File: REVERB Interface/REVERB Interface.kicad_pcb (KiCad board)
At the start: 2 copper layers, 23 parts, among them J1 RPiZeroW, J10 USB, J2 Iridium, J3 APRS, J4 Antenna, J5 MAX3232BOB, J6 USBSER2, J7 USBSER3, J8 USBSER1, J9 USB, M1 MountingHole_Pad, M2 MountingHole_Pad, M3 MountingHole_Pad, M4 MountingHole_Pad, U2 MAX3232, U3 SC16IS752IPW

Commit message: copy old board layout positions
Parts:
- H1, H2, J1, J2, J3: moved to B.Cu
- moved J9 94.0 mm to (164.7, 177.2)
- moved J10 94.0 mm to (160.1, 182.7)
- moved U3 94.0 mm to (177.6, 168.7)
- moved J5 94.0 mm to (141.2, 165.4)
- moved J6 94.0 mm to (136.6, 165.4)
- moved J7 94.0 mm to (160.1, 165.4)
- moved J8 94.0 mm to (132.0, 165.4)
- moved J1 73.6 mm to (168.8, 132.3)
- moved J2 70.9 mm to (123.2, 134.6)
- moved M2 63.1 mm to (189.4, 57.9)
- moved M4 63.1 mm to (191.9, 143.7)
- moved J4 58.1 mm to (114.0, 65.6)
- moved U2 58.1 mm to (141.6, 127.6)
- moved M1 53.5 mm to (115.7, 57.9)
- moved M3 42.1 mm to (111.9, 143.7)
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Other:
- board outline added: 90.2 x 95.9 mm

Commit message: silkscreen labels
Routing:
- added copper zone on B.Cu, net GND
- added copper zone on F.Cu, net GND
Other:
- board text added: ". ."
- board text added: "1 ."
- board text added: "10 9"
- board text added: "12V 12V"
- board text added: "2 G"
- board text added: "3V3 3V3"
- board text added: "4 3"
- board text added: "5V 5V"
- board text added: "7 6"
- board text added: "8 G"
- board text added: "BATV"
- board text added: "BATV BATV"
- board text added: "BCR BCR"
- board text added: "G ."
- board text added: "G 5"
- board text added: "G G"
- board text added: "GND"
- board text added: "PCM PCM"
- board text added: "RX"
- board text added: "SCL"
- board text added: "SDA"
- board text added: "TX"

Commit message: do stuff
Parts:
- removed J5: MAX3232BOB, Connector_PinSocket_2.54mm:PinSocket_1x10_P2.54mm_Vertical
- removed U3: SC16IS752IPW, Package_SO:TSSOP-28_4.4x9.7mm_P0.65mm
- moved J6 79.4 mm to (137.9, 86.1)
- moved J7 79.4 mm to (161.4, 86.1)
- moved J8 79.4 mm to (133.3, 86.1)
- moved J10 42.0 mm to (156.2, 141.0), turned to 90 degrees
- moved J9 39.4 mm to (176.5, 139.7)
- moved C4 19.9 mm to (129.5, 130.8)
- moved C2 19.1 mm to (128.9, 126.8), turned to 270 degrees
- moved C1 17.1 mm to (128.9, 122.6), turned to 90 degrees
- moved C5 10.5 mm to (143.9, 123.2), turned to 270 degrees
- moved C3 5.63 mm to (136.5, 119.4), turned to 270 degrees
- moved U2 4.49 mm to (137.2, 127.0)

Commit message: bunch of work
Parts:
- removed the J7 at (161.4, 86.1)
- removed J8: USBSER1, Connector_PinSocket_2.54mm:PinSocket_1x12_P2.54mm_Vertical
- removed J9: USB, Connector_PinSocket_2.54mm:PinSocket_1x02_P2.54mm_Vertical
- added C6: 4.7uF, Capacitor_SMD:C_0805_2012Metric_Pad1.18x1.45mm_HandSolder, F.Cu at (160.0, 163.8)
- added C7: 0.1uF, Capacitor_SMD:C_0805_2012Metric_Pad1.18x1.45mm_HandSolder, F.Cu at (166.0, 159.1)
- added C8: 1uF, Capacitor_SMD:C_0805_2012Metric_Pad1.18x1.45mm_HandSolder, F.Cu at (160.0, 160.8)
- added D1: RED, LED_SMD:LED_0805_2012Metric_Pad1.15x1.40mm_HandSolder, F.Cu at (164.8, 162.1)
- added D2: GREEN, LED_SMD:LED_0805_2012Metric_Pad1.15x1.40mm_HandSolder, F.Cu at (160.0, 166.9)
- added D3: RED, LED_SMD:LED_0805_2012Metric_Pad1.15x1.40mm_HandSolder, F.Cu at (166.1, 167.6)
- added D4: RED, LED_SMD:LED_0805_2012Metric_Pad1.15x1.40mm_HandSolder, F.Cu at (135.9, 107.9)
- added D5: RED, LED_SMD:LED_0805_2012Metric_Pad1.15x1.40mm_HandSolder, F.Cu at (151.5, 118.7)
- added D6: GREEN, LED_SMD:LED_0805_2012Metric_Pad1.15x1.40mm_HandSolder, F.Cu at (145.4, 111.1)
- added R1: 1K, Resistor_SMD:R_1206_3216Metric_Pad1.30x1.75mm_HandSolder, F.Cu at (166.5, 155.9)
- added R2: 1K, Resistor_SMD:R_1206_3216Metric_Pad1.30x1.75mm_HandSolder, F.Cu at (160.6, 157.7)
- added R3: 1K, Resistor_SMD:R_1206_3216Metric_Pad1.30x1.75mm_HandSolder, F.Cu at (160.6, 154.4)
- added R4: 1K, Resistor_SMD:R_1206_3216Metric_Pad1.30x1.75mm_HandSolder, F.Cu at (130.5, 111.3)
- added R5: 1K, Resistor_SMD:R_1206_3216Metric_Pad1.30x1.75mm_HandSolder, F.Cu at (145.4, 118.7)
- added R6: 1K, Resistor_SMD:R_1206_3216Metric_Pad1.30x1.75mm_HandSolder, F.Cu at (145.4, 115.6)
- added U1: LSM9DS1BOB, REVERB Interface:LSM9DS1BOB, F.Cu at (145.4, 82.5)
- added U3: CY7C65213-28PVXI, Package_SO:SSOP-28_5.3x10.2mm_P0.65mm, F.Cu at (156.4, 132.5)
- J6: value USBSER2 -> USB_B_Micro; footprint Connector_PinSocket_2.54mm:PinSocket_1x12_P2.54mm_Vertical -> REVERB Interface:AdafruitMicroB
- moved J6 59.9 mm to (152.4, 144.1), turned to 180 degrees
- moved J7 27.1 mm to (182.9, 135.9)
- renumbered J10 to J7
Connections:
- H2 pad 19: (no net) -> /SW9
- J6 pad 1: (no net) -> /SW7
- J6 pad 2: (no net) -> /D-
- J6 pad 3: (no net) -> /D+
- J6 pad 5: (no net) -> GND
- J6 pad 6: (no net) -> GND

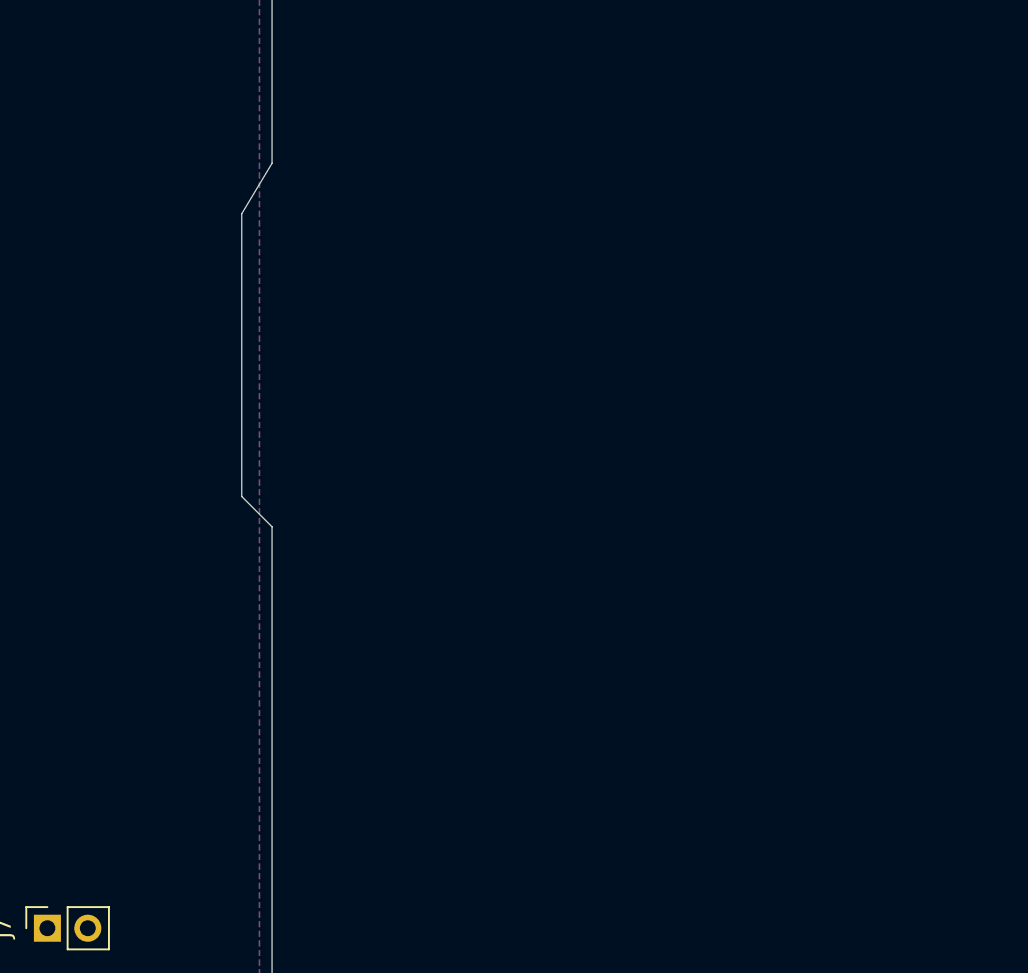
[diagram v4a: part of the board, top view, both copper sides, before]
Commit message: add solder jumpers
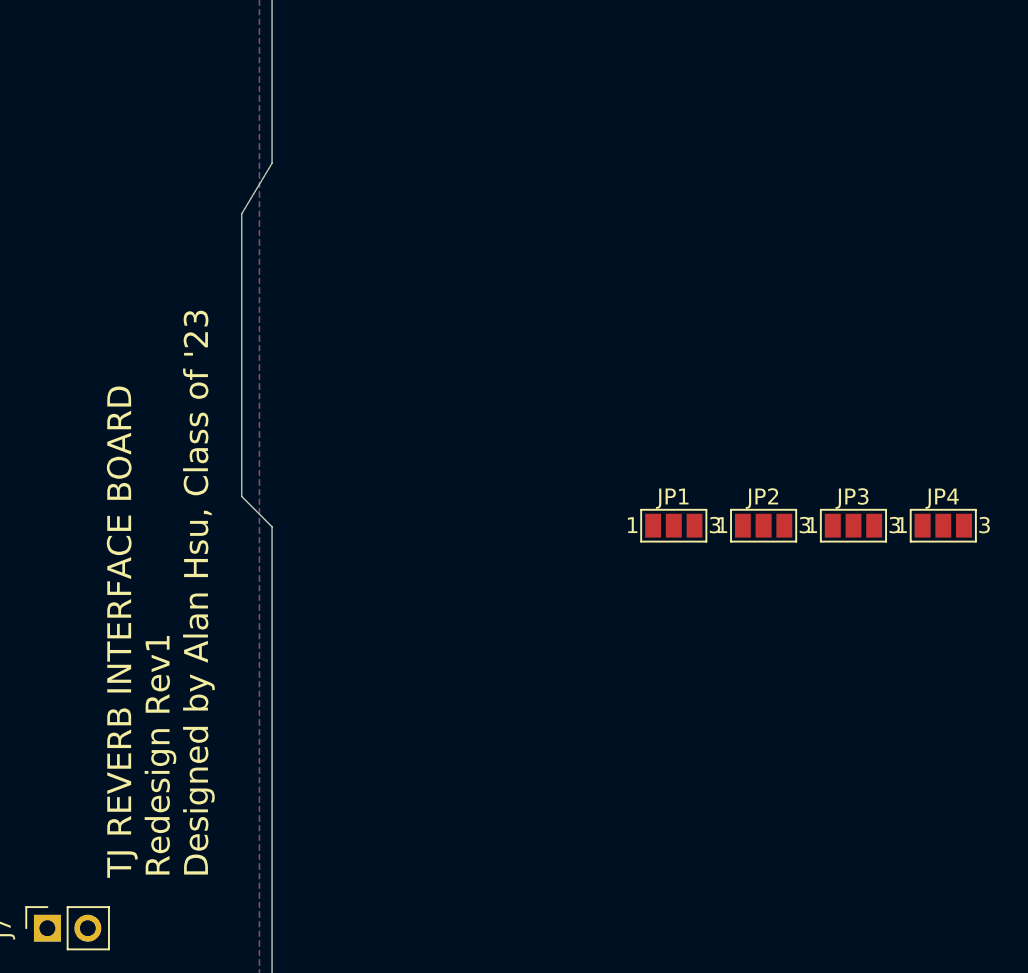
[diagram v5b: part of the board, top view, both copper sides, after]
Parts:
- added JP1: HWRX, Jumper:SolderJumper-3_P1.3mm_Open_Pad1.0x1.5mm_NumberLabels, F.Cu at (222.3, 110.6)
- added JP2: HWTX, Jumper:SolderJumper-3_P1.3mm_Open_Pad1.0x1.5mm_NumberLabels, F.Cu at (227.9, 110.6)
- added JP3: USBUARTRX, Jumper:SolderJumper-3_P1.3mm_Open_Pad1.0x1.5mm_NumberLabels, F.Cu at (233.6, 110.6)
- added JP4: USBUARTTX, Jumper:SolderJumper-3_P1.3mm_Open_Pad1.0x1.5mm_NumberLabels, F.Cu at (239.2, 110.6)
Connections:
- D1 pad 1: /APRSTX -> /USBUARTTX
- D2 pad 1: /APRSRX -> /USBUARTRX
- J1 pad 10: /R1OUT -> /HWRX
- J1 pad 8: /T1IN -> /HWTX
- U3 pad 1: /APRSTX -> /USBUARTTX
- U3 pad 5: /APRSRX -> /USBUARTRX
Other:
- board text added: "TJ REVERB INTERFACE BOARD Redesign Rev1 Designed by Alan Hsu, Class of '23"

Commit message: routing work
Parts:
- R1, R2, R3, R4, R5, R6: footprint Resistor_SMD:R_1206_3216Metric_Pad1.30x1.75mm_HandSolder -> Resistor_SMD:R_0805_2012Metric_Pad1.20x1.40mm_HandSolder
- moved D3 101.4 mm to (137.2, 70.5), turned to 180 degrees
- moved R3 88.8 mm to (131.4, 70.6)
- moved JP1 82.3 mm to (140.4, 102.3)
- moved JP2 82.3 mm to (146.0, 102.3)
- moved JP3 82.3 mm to (151.7, 102.3)
- moved JP4 82.3 mm to (157.3, 102.3)
- moved R4 40.1 mm to (142.9, 73.2)
- moved D4 38.7 mm to (142.9, 69.8)
- moved D2 37.4 mm to (136.5, 137.8), turned to 270 degrees
- moved C6 35.9 mm to (149.2, 129.5), turned to 270 degrees
- moved C7 35.6 mm to (146.1, 129.5), turned to 270 degrees
- moved D1 31.5 mm to (144.8, 137.8), turned to 270 degrees
- moved R2 28.8 mm to (139.7, 137.8), turned to 270 degrees
- moved R1 26.0 mm to (148.0, 137.8), turned to 270 degrees
- moved C8 24.0 mm to (163.8, 137.2), turned to 270 degrees
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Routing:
- net +5V: track 0.00 -> 95.2 mm
- net /SW7: track 0.00 -> 15.8 mm
- net GND: track 0.00 -> 10.4 mm
- net /D-: track 0.00 -> 9.60 mm
- net /D+: track 0.00 -> 8.49 mm
- net Net-(C3-Pad2): track 0.00 -> 6.37 mm
- net Net-(C4-Pad2): track 0.00 -> 4.77 mm
- net Net-(C8-Pad1): track 0.00 -> 4.72 mm
- net Net-(C1-Pad1): track 0.00 -> 4.25 mm
- net Net-(C2-Pad2): track 0.00 -> 4.05 mm
- net Net-(C1-Pad2): track 0.00 -> 4.05 mm
- net Net-(C2-Pad1): track 0.00 -> 3.72 mm
- net /SW8: track 0.00 -> 3.16 mm
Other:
- board text added: "Programming USB Header"
- board text added: "THIS SIDE DOWN"
- board text added: "THIS SIDE UP"

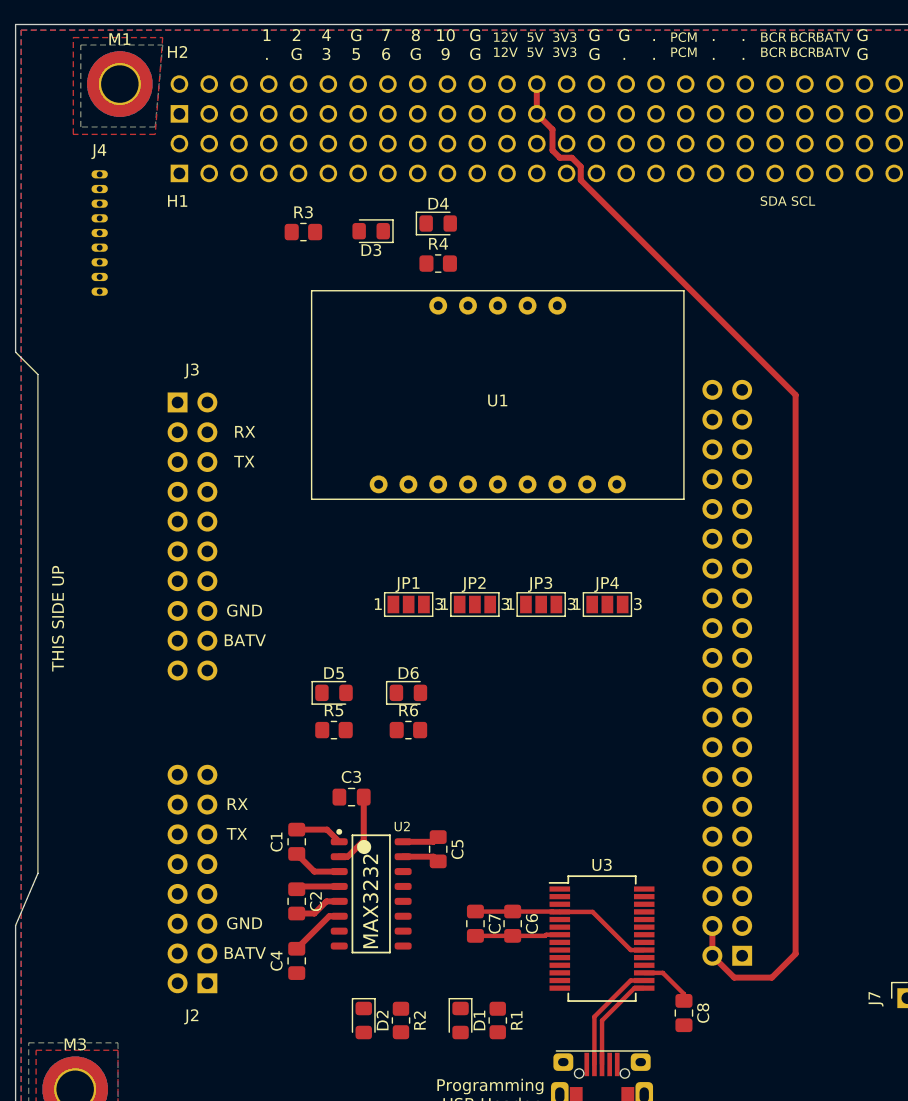
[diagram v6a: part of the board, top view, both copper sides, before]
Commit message: Update REVERB Interface.kicad_pcb
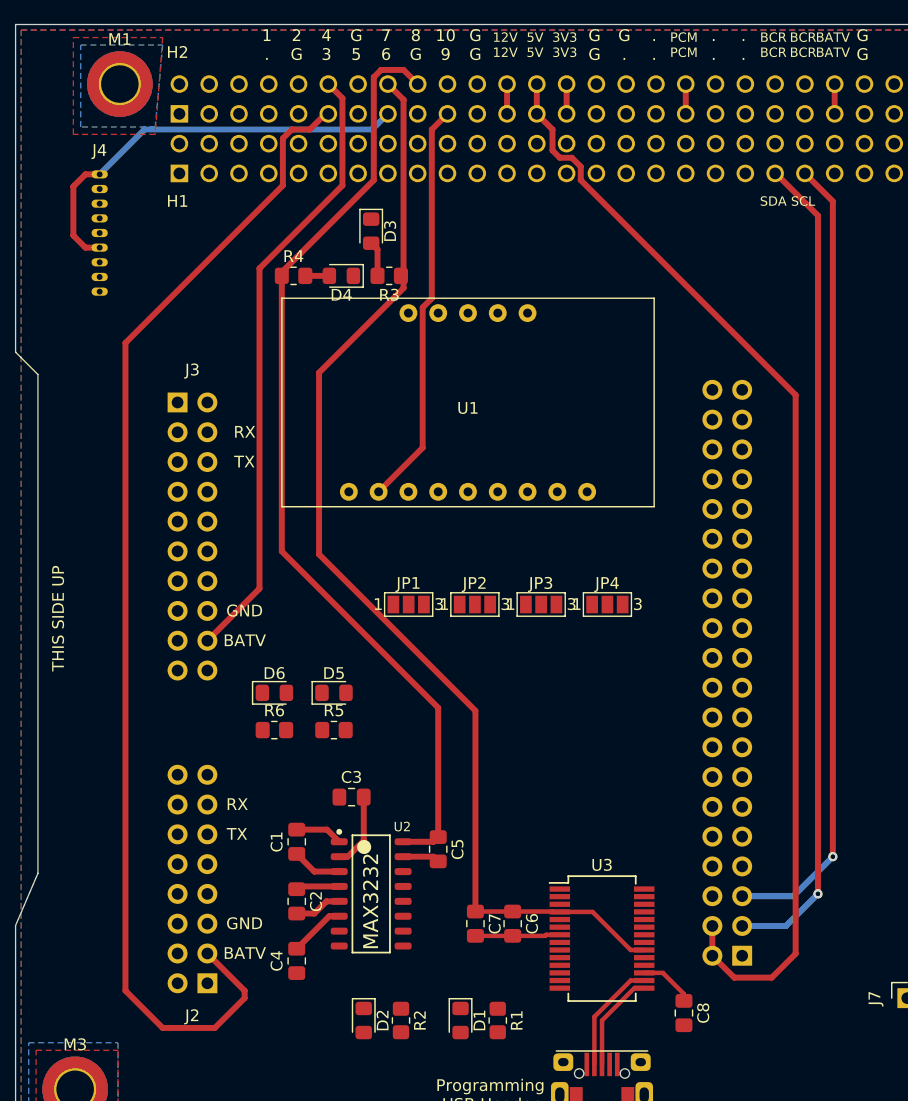
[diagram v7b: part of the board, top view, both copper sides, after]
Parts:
- moved R4 12.4 mm to (130.5, 74.3)
- moved D6 11.4 mm to (128.9, 109.9)
- moved R6 11.4 mm to (128.9, 113.0)
- moved D4 9.39 mm to (134.6, 74.3), turned to 180 degrees
- moved R3 8.22 mm to (138.7, 74.3), turned to 180 degrees
- moved U1 2.62 mm to (145.4, 85.1)
- turned D3 to 270 degrees
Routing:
- net /SW3: track 0.00 -> 100.6 mm
- net /SW7: track 15.8 -> 95.4 mm
- net /SW8: track 3.16 -> 81.2 mm
- net /EPSSDA: track 0.00 -> 70.6 mm, vias 0 -> 1
- net /EPSSCL: track 0.00 -> 68.4 mm, vias 0 -> 1
- net /SW4: track 0.00 -> 52.7 mm
- net /SW6: track 0.00 -> 36.2 mm
- net /SW9: track 0.00 -> 34.7 mm
- net Net-(D3-Pad2): track 0.00 -> 3.01 mm
- net VBUS: track 0.00 -> 2.54 mm
- net /PCM_IN: track 0.00 -> 2.54 mm
- net +3V3: track 0.00 -> 2.54 mm
- net +12V: track 0.00 -> 2.54 mm
- net Net-(D4-Pad2): track 0.00 -> 2.06 mm

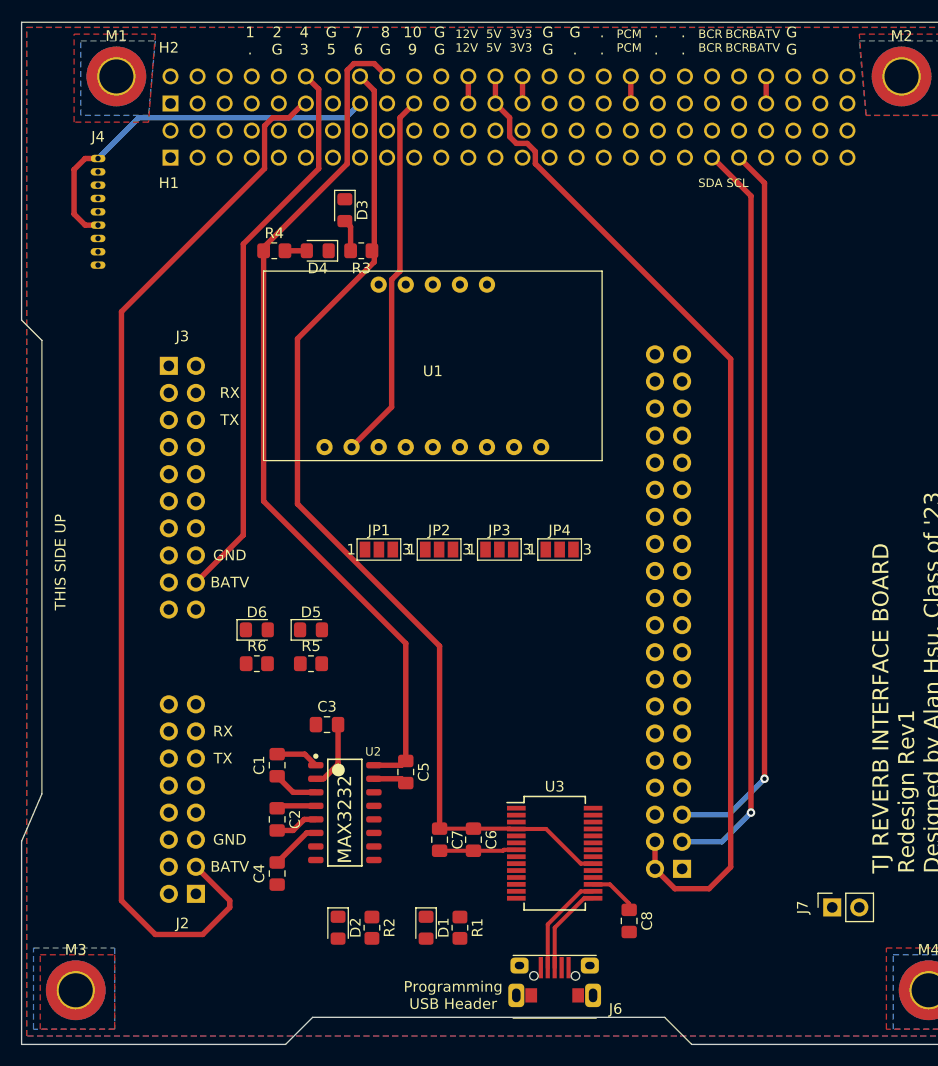
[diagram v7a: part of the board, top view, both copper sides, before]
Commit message: finsihing up routing
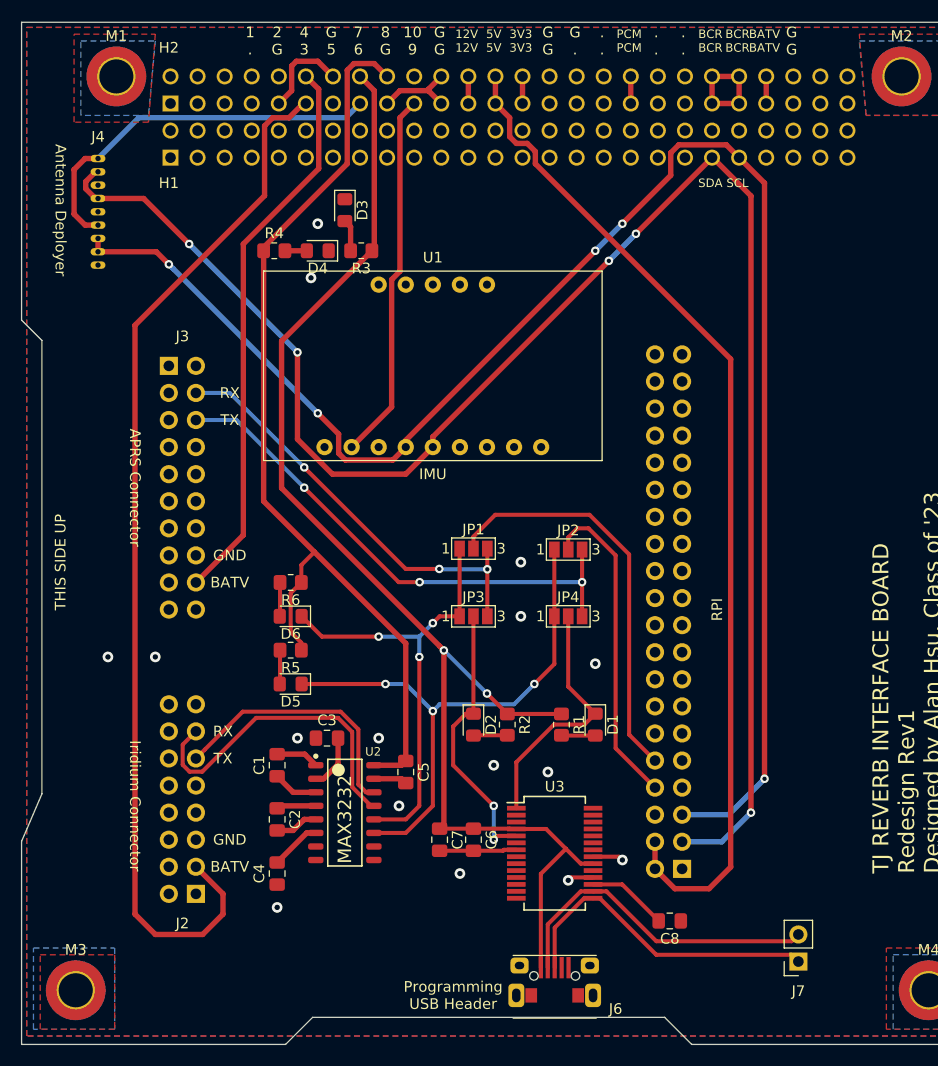
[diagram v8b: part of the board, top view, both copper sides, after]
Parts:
- moved D1 24.8 mm to (160.7, 118.7)
- moved R2 22.9 mm to (152.4, 118.7)
- moved D2 22.9 mm to (149.2, 118.7)
- moved R1 21.3 mm to (157.5, 118.7)
- moved JP2 12.1 mm to (158.1, 102.3)
- moved JP1 8.87 mm to (149.2, 102.2)
- moved R6 8.26 mm to (132.1, 105.4), turned to 180 degrees
- moved JP3 6.72 mm to (149.2, 108.6)
- moved JP4 6.32 mm to (158.1, 108.6)
- moved J7 5.99 mm to (179.7, 141.0), turned to 180 degrees
- moved D5 5.43 mm to (132.1, 114.9), turned to 180 degrees
- moved C8 3.81 mm to (167.6, 137.2), turned to 0 degrees
- moved D6 3.42 mm to (132.1, 108.6), turned to 180 degrees
- moved R5 2.29 mm to (132.1, 111.8), turned to 180 degrees
- moved C3 1.27 mm to (135.5, 120.0)
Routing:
- net /EPSSDA: track 70.6 -> 160.3 mm, vias 1 -> 5
- net /EPSSCL: track 68.4 -> 153.3 mm, vias 1 -> 5
- net /T1IN: track 0.00 -> 52.8 mm, vias 0 -> 3
- net /APRSTX: track 0.00 -> 48.8 mm, vias 0 -> 3
- net /R1OUT: track 0.00 -> 43.4 mm, vias 0 -> 3
- net /APRSRX: track 0.00 -> 40.5 mm, vias 0 -> 3
- net /HWRX: track 0.00 -> 38.5 mm
- net /R1IN: track 0.00 -> 30.4 mm
- net /HWTX: track 0.00 -> 30.3 mm
- net /SW7: track 95.4 -> 122.6 mm, vias 0 -> 2
- net /USBUARTRX: track 0.00 -> 26.0 mm, vias 0 -> 2
- net /T1OUT: track 0.00 -> 24.7 mm
- net /USBUARTTX: track 0.00 -> 23.8 mm
- net GND: track 10.4 -> 32.3 mm, vias 0 -> 16
- net /D+: track 8.49 -> 30.2 mm
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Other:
- board text added: "APRS Connector"
- board text added: "Antenna Deployer"
- board text added: "IMU"
- board text added: "Iridium Connector"
- board text added: "RPI"
